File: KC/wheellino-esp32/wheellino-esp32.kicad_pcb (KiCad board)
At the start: 2 copper layers, 33 parts, among them J1 SR04, J2 Servo, J3 Motor Drivers, J4 Motor Sensors, J5 Contact Sensors, J6 12V, J7 5V, J8 GY521, J9 LCD, U1 3V3

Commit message: Esp32 board
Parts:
- removed the REF** at (124.5, 83.8)
- added C7: 1n, Capacitor_THT:C_Rect_L7.0mm_W2.0mm_P5.00mm, F.Cu at (172.7, 61.0)
- added C8: 1n, Capacitor_THT:C_Rect_L7.0mm_W2.0mm_P5.00mm, F.Cu at (170.0, 61.0)
- added R8: 10K, Resistor_THT:R_Axial_DIN0207_L6.3mm_D2.5mm_P10.16mm_Horizontal, F.Cu at (162.6, 91.4)
- added R9: 10K, Resistor_THT:R_Axial_DIN0207_L6.3mm_D2.5mm_P10.16mm_Horizontal, F.Cu at (162.6, 66.0)
- added U2: ESP32-DevKitC, Whellino:ESP32, F.Cu at (175.3, 68.6)
- C6: value 1n -> 22uF; footprint Capacitor_THT:C_Rect_L7.0mm_W2.0mm_P5.00mm -> Capacitor_THT:CP_Radial_D5.0mm_P2.50mm
- R1, R2, R3, R4, R7: value 1K -> 220
- R5: value 10K -> 100K
- R6: value 2K -> 22K
- moved R5 113.4 mm to (205.7, 61.1), turned to 180 degrees
- moved J6 108.5 mm to (190.5, 53.3), turned to 90 degrees
- moved R6 101.7 mm to (195.6, 63.5)
- moved C5 95.6 mm to (190.5, 61.0), turned to 180 degrees
- moved J7 94.9 mm to (180.3, 53.3), turned to 90 degrees
- moved R7 72.7 mm to (154.9, 68.6), turned to 180 degrees
- moved R2 67.1 mm to (154.9, 71.1), turned to 180 degrees
- moved D5 65.5 mm to (127.0, 63.5), turned to 0 degrees
- moved D1 63.7 mm to (127.0, 71.1), turned to 0 degrees
- moved R1 62.3 mm to (154.9, 73.7), turned to 180 degrees
- moved D2 61.2 mm to (137.2, 71.1), turned to 0 degrees
- moved R3 58.0 mm to (154.9, 76.2), turned to 180 degrees
- moved D3 53.4 mm to (127.0, 78.7), turned to 0 degrees
- moved R4 52.4 mm to (155.0, 78.7), turned to 180 degrees
- moved D4 50.4 mm to (137.2, 78.7), turned to 0 degrees
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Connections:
- C6 pad 1: +3V3 -> Net-(U2-CHIP_PU)
- J1 pad 1: unconnected-(J1-Pin_1-Pad1) -> +5VD
- J1 pad 2: unconnected-(J1-Pin_2-Pad2) -> Net-(J1-Pin_2)
- J1 pad 3: unconnected-(J1-Pin_3-Pad3) -> Net-(J1-Pin_3)
- J1 pad 4: unconnected-(J1-Pin_4-Pad4) -> GND
- J2 pad 1: unconnected-(J2-Pin_1-Pad1) -> GND
- J2 pad 2: unconnected-(J2-Pin_2-Pad2) -> +5VD
- J2 pad 3: unconnected-(J2-Pin_3-Pad3) -> Net-(J2-Pin_3)
- J3 pad 1: unconnected-(J3-Pin_1-Pad1) -> Net-(J3-Pin_1)
- J3 pad 2: unconnected-(J3-Pin_2-Pad2) -> +5VD
- J3 pad 3: unconnected-(J3-Pin_3-Pad3) -> Net-(J3-Pin_3)
- J3 pad 4: unconnected-(J3-Pin_4-Pad4) -> GND
- J3 pad 5: unconnected-(J3-Pin_5-Pad5) -> Net-(J3-Pin_5)
- J3 pad 6: unconnected-(J3-Pin_6-Pad6) -> GND
- J3 pad 7: unconnected-(J3-Pin_7-Pad7) -> Net-(J3-Pin_7)
- J3 pad 8: unconnected-(J3-Pin_8-Pad8) -> +5VD
- J4 pad 1: unconnected-(J4-Pin_1-Pad1) -> +3V3
- J4 pad 2: unconnected-(J4-Pin_2-Pad2) -> +3V3
- J4 pad 3: unconnected-(J4-Pin_3-Pad3) -> GND
- J4 pad 4: unconnected-(J4-Pin_4-Pad4) -> GND
- J4 pad 5: unconnected-(J4-Pin_5-Pad5) -> Net-(J4-Pin_5)
- J4 pad 6: unconnected-(J4-Pin_6-Pad6) -> Net-(J4-Pin_6)
- J5 pad 1: unconnected-(J5-Pin_1-Pad1) -> Net-(J5-Pin_1)
- J5 pad 2: unconnected-(J5-Pin_2-Pad2) -> GND
- J5 pad 3: unconnected-(J5-Pin_3-Pad3) -> Net-(J5-Pin_3)
- J5 pad 4: unconnected-(J5-Pin_4-Pad4) -> GND
- J8 pad 3: unconnected-(J8-Pin_3-Pad3) -> Net-(J8-Pin_3)
- J8 pad 4: unconnected-(J8-Pin_4-Pad4) -> Net-(J8-Pin_4)
- J9 pad 1: unconnected-(J9-Pin_1-Pad1) -> Net-(J8-Pin_3)
- J9 pad 2: unconnected-(J9-Pin_2-Pad2) -> Net-(J8-Pin_4)
- J9 pad 3: unconnected-(J9-Pin_3-Pad3) -> +5VD
- J9 pad 4: unconnected-(J9-Pin_4-Pad4) -> GND
- R1 pad 1: unconnected-(R1-Pad1) -> Net-(J3-Pin_3)
- R2 pad 1: unconnected-(R2-Pad1) -> Net-(J3-Pin_1)
- R3 pad 1: unconnected-(R3-Pad1) -> Net-(J3-Pin_5)
- R4 pad 1: unconnected-(R4-Pad1) -> Net-(J3-Pin_7)
- R7 pad 1: unconnected-(R7-Pad1) -> Net-(U2-DAC_1/ADC2_CH8/GPIO25)
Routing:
- net GND: track 0.00 -> 399.6 mm
- net +5VD: track 0.00 -> 233.7 mm
- net +3V3: track 0.00 -> 159.7 mm
- net Net-(J3-Pin_1): track 0.00 -> 104.2 mm, vias 0 -> 1
- net Net-(J1-Pin_2): track 0.00 -> 94.9 mm
- net Net-(J8-Pin_3): track 0.00 -> 91.2 mm, vias 0 -> 2
- net Net-(J3-Pin_5): track 0.00 -> 90.9 mm, vias 0 -> 1
- net Net-(J8-Pin_4): track 0.00 -> 88.6 mm, vias 0 -> 2
- net Net-(J3-Pin_3): track 0.00 -> 88.2 mm, vias 0 -> 1
- net Net-(J3-Pin_7): track 0.00 -> 86.9 mm, vias 0 -> 1
- net Net-(J2-Pin_3): track 0.00 -> 63.0 mm
- net Net-(J1-Pin_3): track 0.00 -> 58.0 mm
- net Net-(J4-Pin_5): track 0.00 -> 54.4 mm, vias 0 -> 3
- net Net-(J4-Pin_6): track 0.00 -> 47.9 mm
- net Net-(J5-Pin_3): track 0.00 -> 44.7 mm
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- added copper zone on B.Cu, net GND
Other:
- board outline added: 91.4 x 71.1 mm

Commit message: Changed
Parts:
- moved C2 2.54 mm to (149.9, 111.8)
- moved C3 2.54 mm to (160.0, 111.8)
- moved C6 2.54 mm to (172.7, 71.1)
- moved J3 2.54 mm to (149.9, 53.3)
- moved U2 2.54 mm to (177.8, 68.6)
- moved C1 2.54 mm to (144.8, 109.2)
- moved C4 2.54 mm to (165.1, 109.2)
- moved C7 2.54 mm to (175.3, 61.0)
- moved C8 2.54 mm to (172.6, 61.0)
- moved D1 2.54 mm to (129.5, 71.1)
- moved D2 2.54 mm to (139.7, 71.1)
- moved D3 2.54 mm to (129.5, 78.7)
- moved D4 2.54 mm to (139.7, 78.7)
- moved D5 2.54 mm to (129.5, 63.5)
- moved J1 2.54 mm to (137.2, 50.8)
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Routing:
- net GND: track 399.6 -> 393.5 mm
- net +12V: track 18.4 -> 16.0 mm
- net Net-(U2-SENSOR_VN/GPIO39/ADC1_CH3): track 29.1 -> 28.1 mm

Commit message: reordered
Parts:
- removed the C7 at (175.3, 61.0)
- removed the C8 at (172.6, 61.0)
- added C1: 1uF, Capacitor_THT:CP_Radial_D5.0mm_P2.50mm, F.Cu at (175.3, 61.0)
- added C2: 1uF, Capacitor_THT:CP_Radial_D5.0mm_P2.50mm, F.Cu at (172.7, 61.0)
- moved U2 5.10 mm to (157.5, 106.7), turned to -90 degrees
- renumbered C5 to C3, C6 to C4, C1 to C5, C2 to C6, C3 to C7, C4 to C8, J4 to J1, J5 to J2, J1 to J3, J2 to J4, J8 to J5, J3 to J6, J9 to J7, J6 to J8, J7 to J9, R8 to R1, R9 to R2, R5 to R3, R6 to R4, R1 to R5, R2 to R6, R3 to R7, R4 to R8, R7 to R9, U2 to U1, U1 to U2
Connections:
- U2 pad 2: GND -> +3V3
- U2 pad 3: +3V3 -> GND
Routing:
- net GND: track 393.5 -> 398.7 mm
- net +5VD: track 233.7 -> 236.6 mm
- net +3V3: track 159.7 -> 160.7 mm

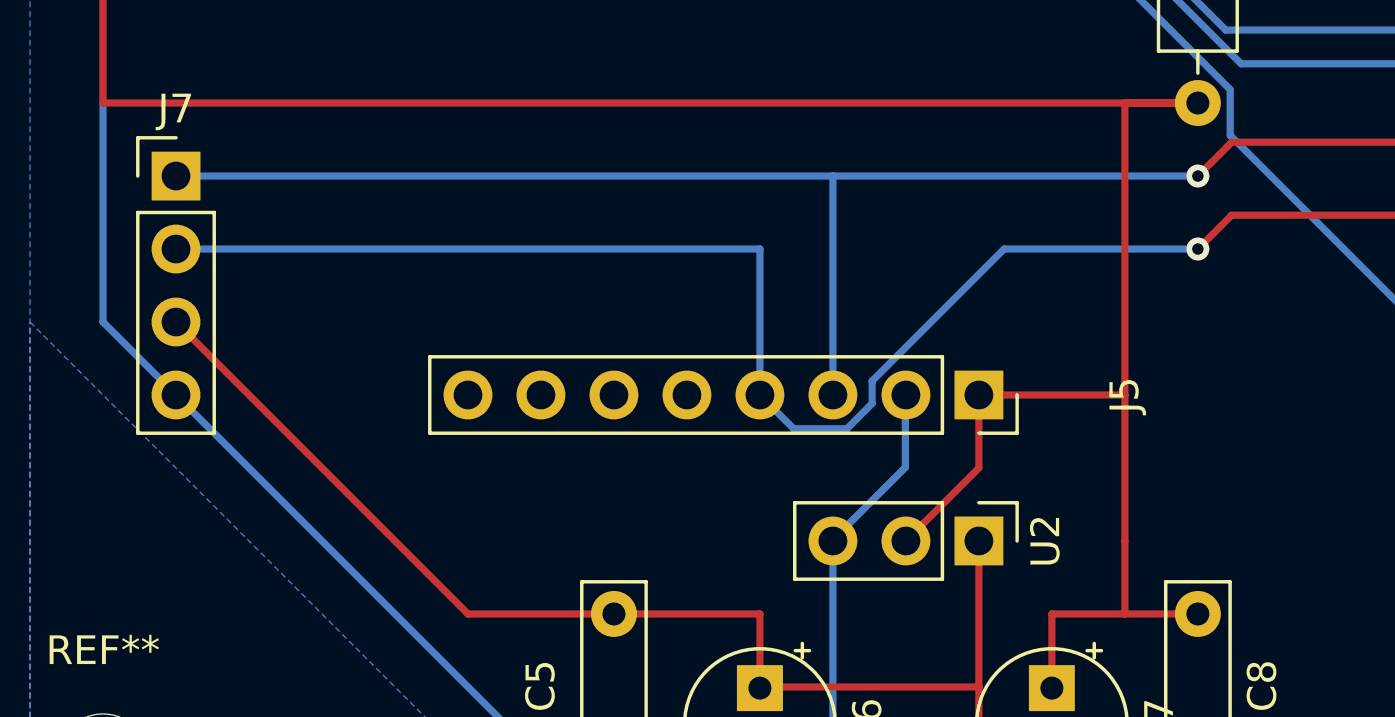
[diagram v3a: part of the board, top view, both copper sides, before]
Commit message: Fixed pcb error
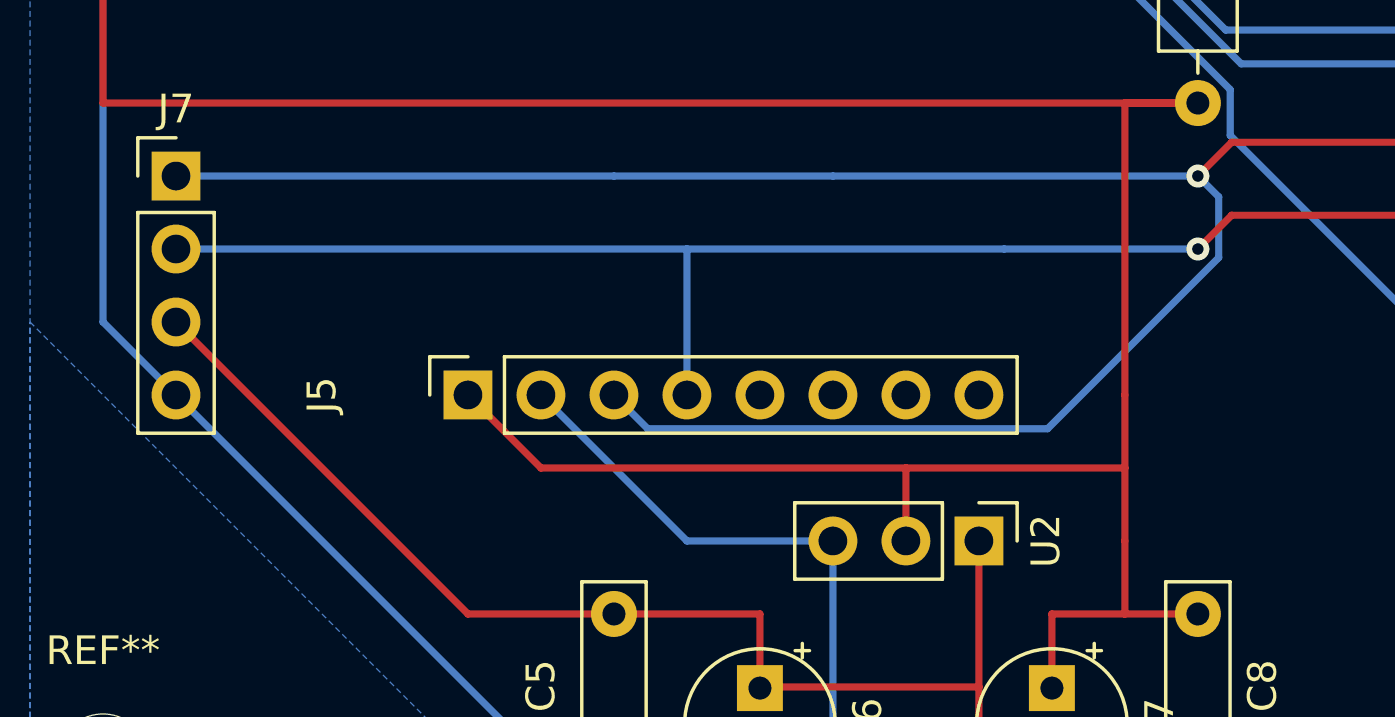
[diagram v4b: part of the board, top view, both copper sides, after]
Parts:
- moved J5 17.8 mm to (139.7, 101.6), turned to 90 degrees
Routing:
- net Net-(J5-Pin_3): track 91.2 -> 110.7 mm
- net +3V3: track 160.7 -> 175.9 mm
- net GND: track 398.7 -> 404.8 mm
- net Net-(J5-Pin_4): track 88.6 -> 85.1 mm

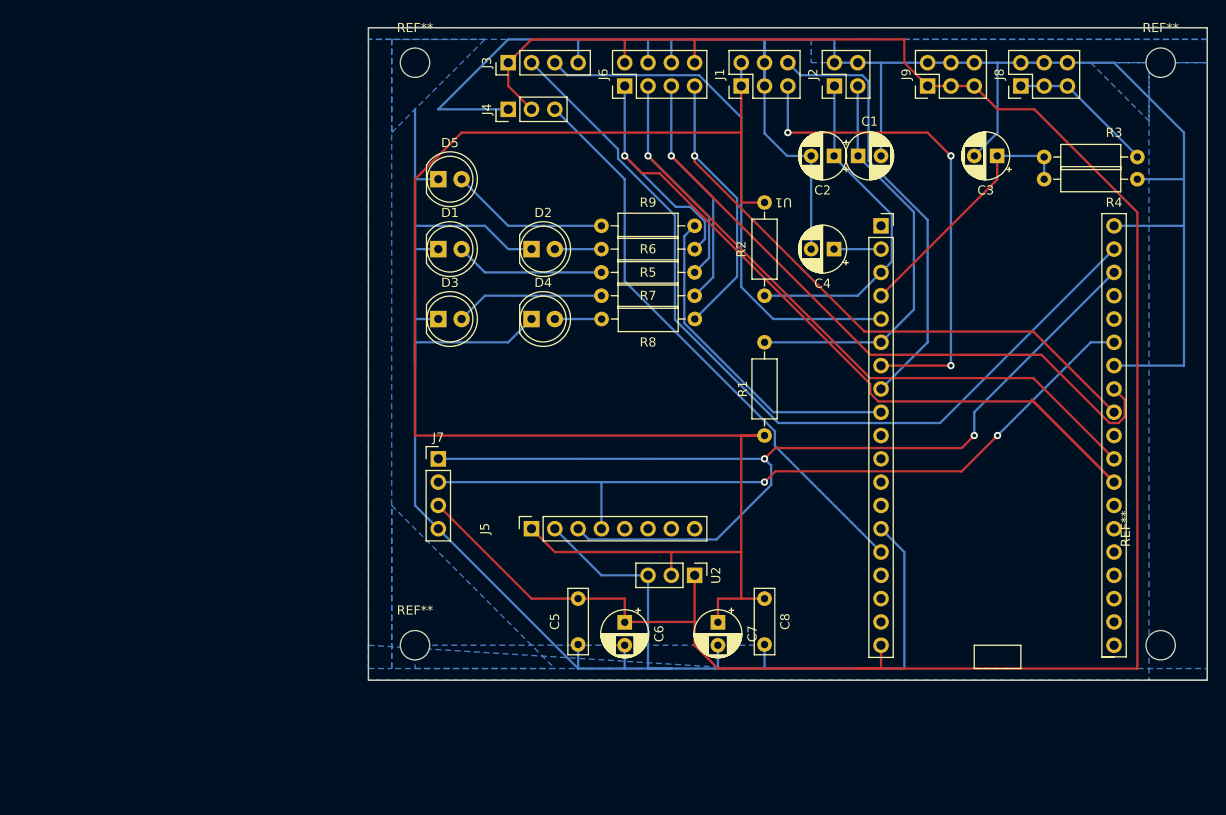
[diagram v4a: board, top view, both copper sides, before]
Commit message: flip camera image Lidar signals LidarServo head cad projects Add lidar
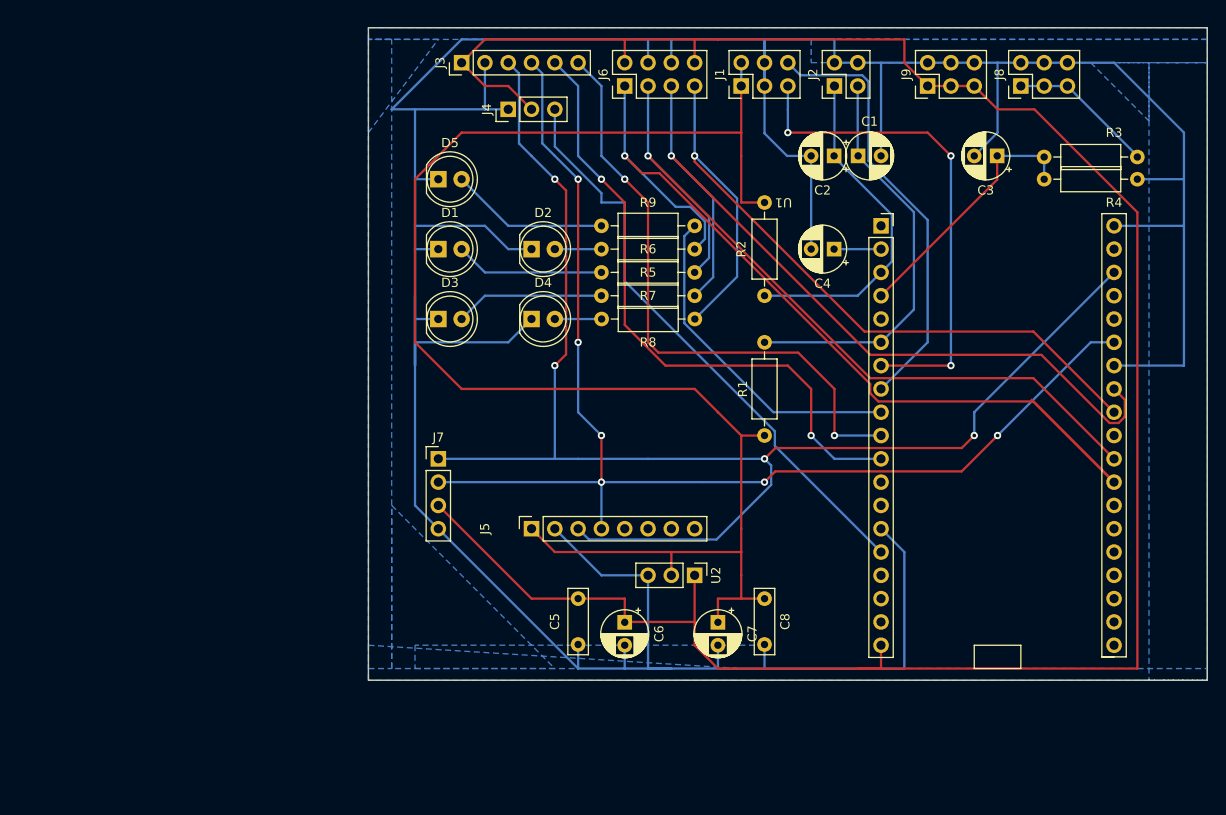
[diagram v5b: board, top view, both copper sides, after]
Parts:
- removed REF** (x4): MountingHole_3.2mm_M3_DIN965, MountingHole:MountingHole_3.2mm_M3_DIN965
- J3: footprint Connector_PinHeader_2.54mm:PinHeader_1x04_P2.54mm_Vertical -> Connector_PinHeader_2.54mm:PinHeader_1x06_P2.54mm_Vertical
- moved J3 5.08 mm to (132.1, 50.8)
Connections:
- J3 pad 2: Net-(J3-Pin_2) -> GND
- J3 pad 4: GND -> Net-(J3-Pin_4)
- J5 pad 3: Net-(J5-Pin_3) -> Net-(J3-Pin_3)
- J5 pad 4: Net-(J5-Pin_4) -> Net-(J3-Pin_4)
- J7 pad 1: Net-(J5-Pin_3) -> Net-(J3-Pin_3)
- J7 pad 2: Net-(J5-Pin_4) -> Net-(J3-Pin_4)
- U1 pad 10: unconnected-(U1-DAC_2/ADC2_CH9/GPIO26-Pad10) -> Net-(J3-Pin_6)
- U1 pad 11: unconnected-(U1-ADC2_CH7/GPIO27-Pad11) -> Net-(J3-Pin_5)
- U1 pad 33: Net-(J5-Pin_4) -> Net-(J3-Pin_4)
- U1 pad 36: Net-(J5-Pin_3) -> Net-(J3-Pin_3)
- U1 pad 37: Net-(J3-Pin_2) -> unconnected-(U1-GPIO23-Pad37)
- U1 pad 5: Net-(J3-Pin_3) -> unconnected-(U1-VDET_1/GPIO34/ADC1_CH6-Pad5)
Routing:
- net Net-(J3-Pin_4): track 0.00 -> 133.9 mm, vias 0 -> 6
- net Net-(J5-Pin_3): track 110.7 -> 0.00 mm, vias 2 -> 0
- net Net-(J3-Pin_3): track 58.0 -> 157.0 mm, vias 0 -> 4
- net Net-(J3-Pin_2): track 94.9 -> 0.00 mm
- net Net-(J5-Pin_4): track 85.1 -> 0.00 mm, vias 2 -> 0
- net Net-(J3-Pin_5): track 0.00 -> 68.7 mm, vias 0 -> 2
- net Net-(J3-Pin_6): track 0.00 -> 66.2 mm, vias 0 -> 2
- net GND: track 404.8 -> 417.5 mm
- net +5VD: track 236.6 -> 245.3 mm
- net +3V3: track 175.9 -> 167.4 mm
- net Net-(J4-Pin_3): track 63.0 -> 64.5 mm
